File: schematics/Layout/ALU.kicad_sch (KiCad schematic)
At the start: 11 parts

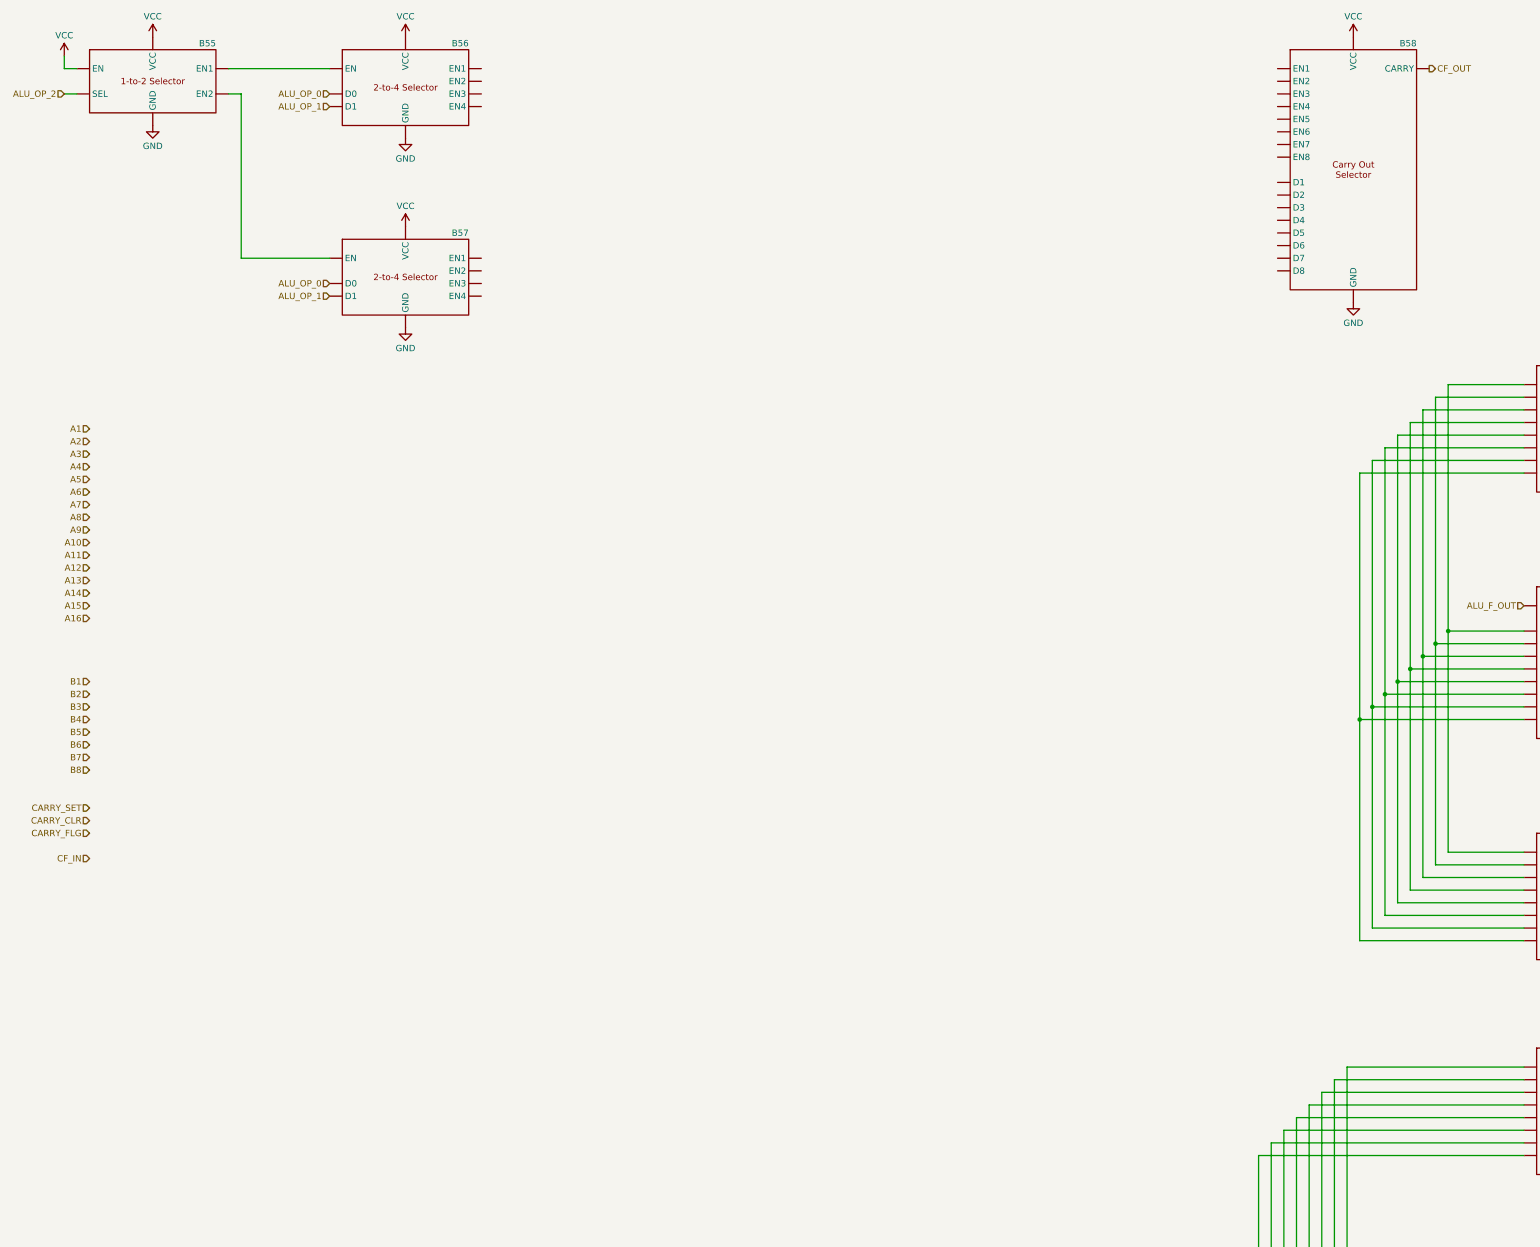
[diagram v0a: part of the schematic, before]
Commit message: Update layout to KiCad 9.0.1, add adder portion of ALU, add 2 bit adder component.
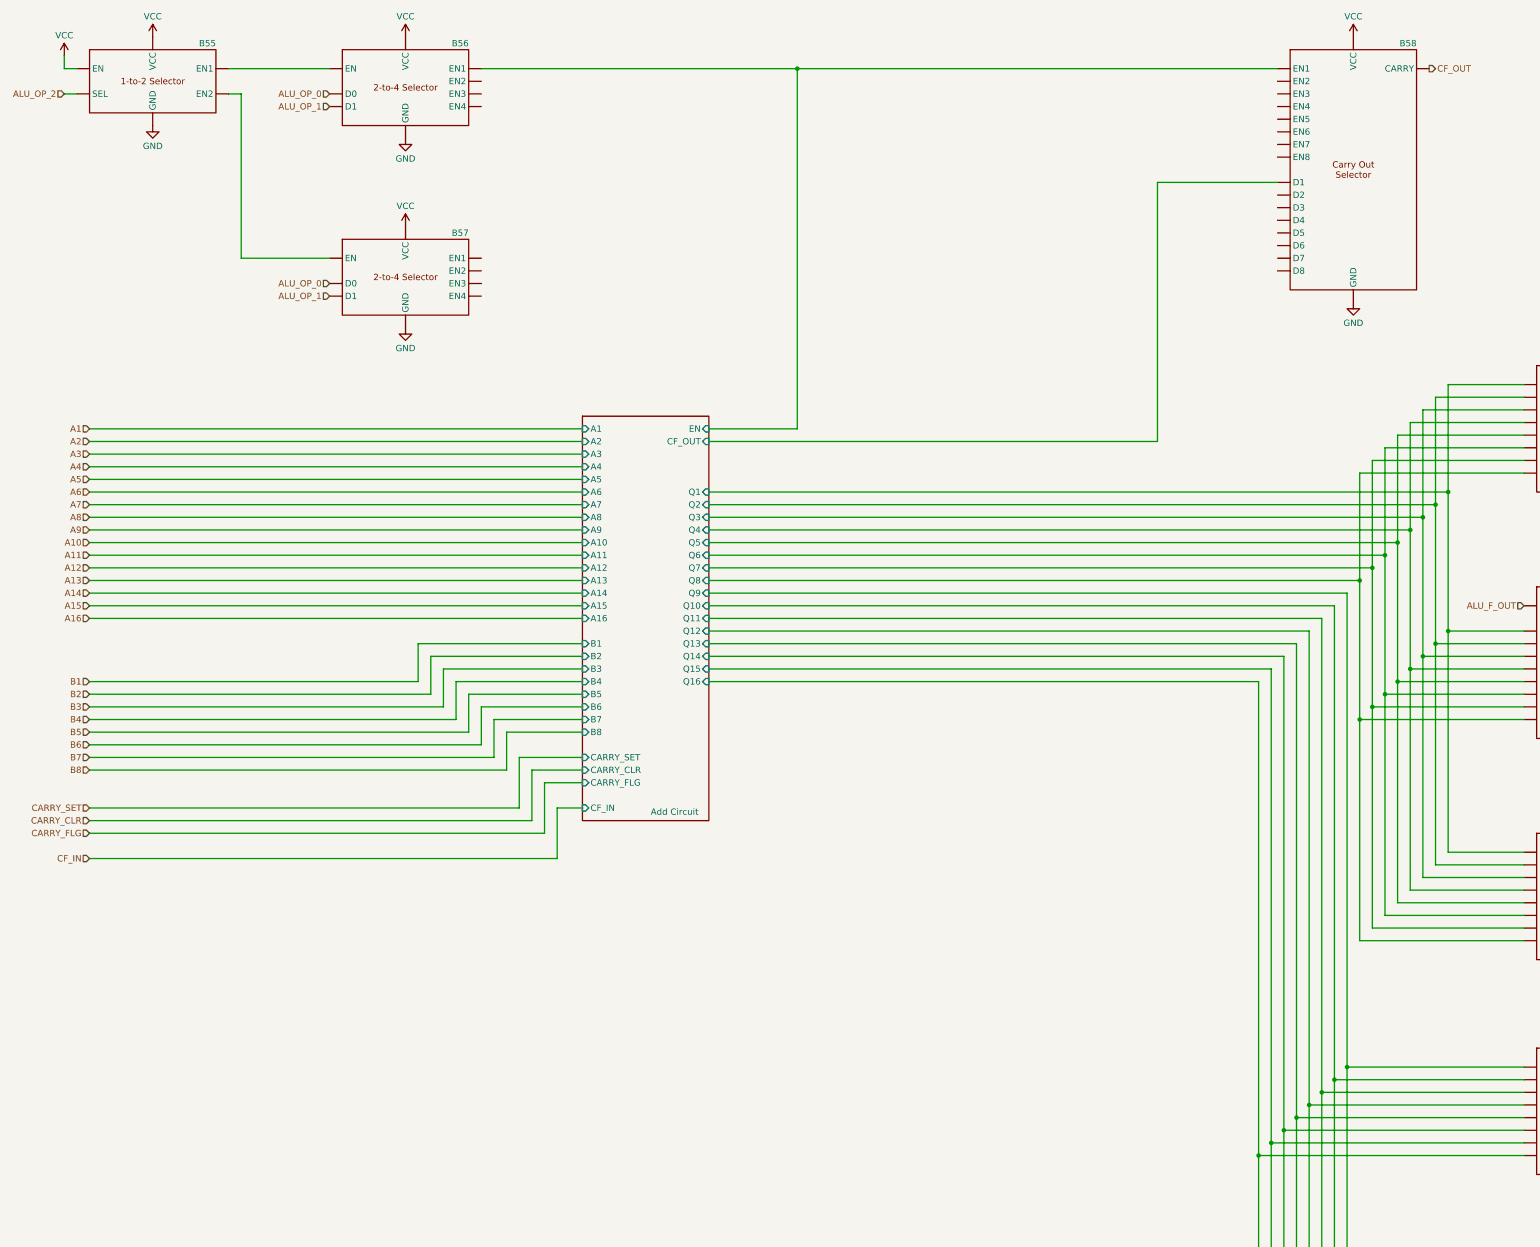
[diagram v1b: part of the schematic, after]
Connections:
- new net: B55. (EN2), B57. (EN4)
- new net: B55. (EN2), B56. (EN4)
- new net: B59. (NONZERO), B60. (OUT)
- new net Add Circuit/CF_OUT: B58. (CARRY)
- new net Add Circuit/EN: B56. (EN4), B58. (CARRY)
- new net Add Circuit/Q1: B59. (NONZERO), B61. (GND), B63. (OUT8)
- new net Add Circuit/Q10: B62. (GND), B64. (OUT8), B65. (OUT8)
- new net Add Circuit/Q11: B62. (GND), B64. (OUT8), B65. (OUT8)
- new net Add Circuit/Q12: B62. (GND), B64. (OUT8), B65. (OUT8)
- new net Add Circuit/Q13: B62. (GND), B64. (OUT8), B65. (OUT8)
- new net Add Circuit/Q14: B62. (GND), B64. (OUT8), B65. (OUT8)
- new net Add Circuit/Q15: B62. (GND), B64. (OUT8), B65. (OUT8)
- new net Add Circuit/Q16: B62. (GND), B64. (OUT8), B65. (OUT8)
- new net Add Circuit/Q2: B59. (NONZERO), B61. (GND), B63. (OUT8)
- new net Add Circuit/Q3: B59. (NONZERO), B61. (GND), B63. (OUT8)
- new net Add Circuit/Q4: B59. (NONZERO), B61. (GND), B63. (OUT8)
- new net Add Circuit/Q5: B59. (NONZERO), B61. (GND), B63. (OUT8)
- new net Add Circuit/Q6: B59. (NONZERO), B61. (GND), B63. (OUT8)
- new net Add Circuit/Q7: B59. (NONZERO), B61. (GND), B63. (OUT8)
- new net Add Circuit/Q8: B59. (NONZERO), B61. (GND), B63. (OUT8)
- new net Add Circuit/Q9: B62. (GND), B64. (OUT8), B65. (OUT8)
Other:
- added sheet Add Circuit (ALU Add Circuit.kicad_sch)

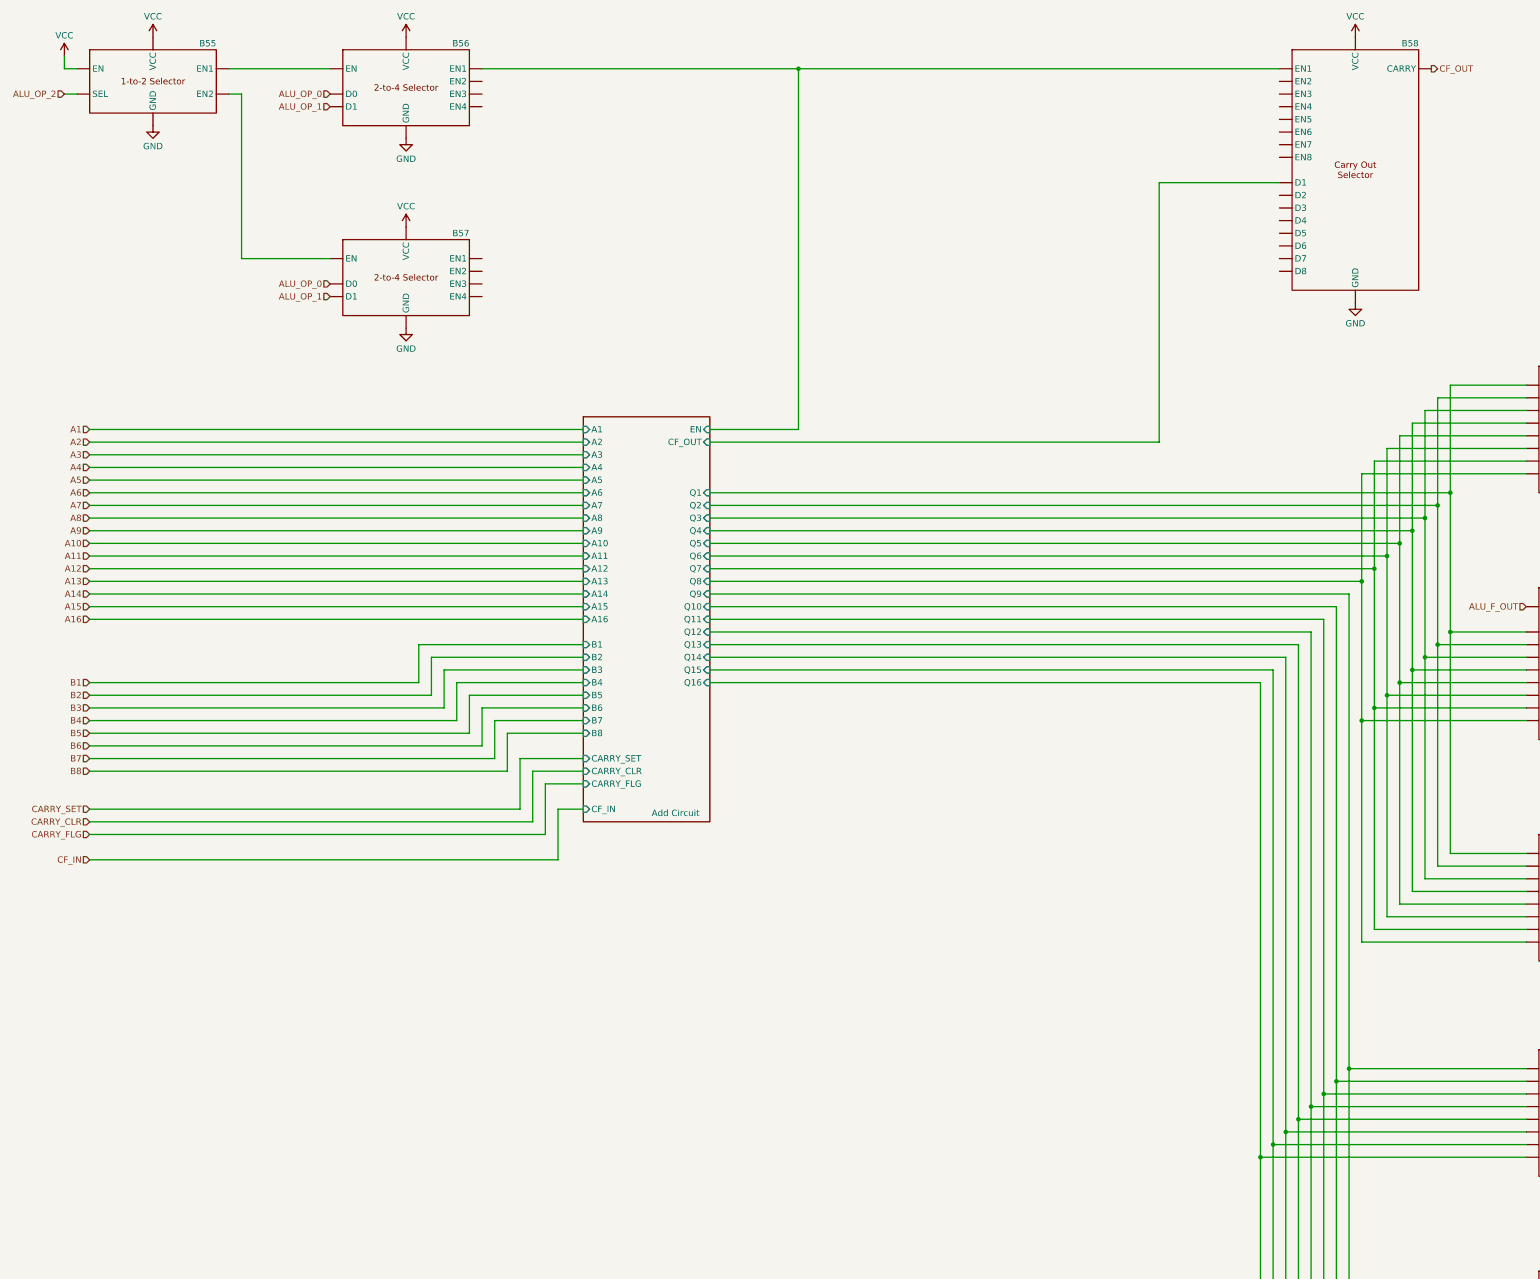
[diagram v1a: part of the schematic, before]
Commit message: Diagram boolean logic board under ALU, new instruction decoder board. Fix backwards ALU opcode decode leftover from swapping to positive instead of inverted signals.
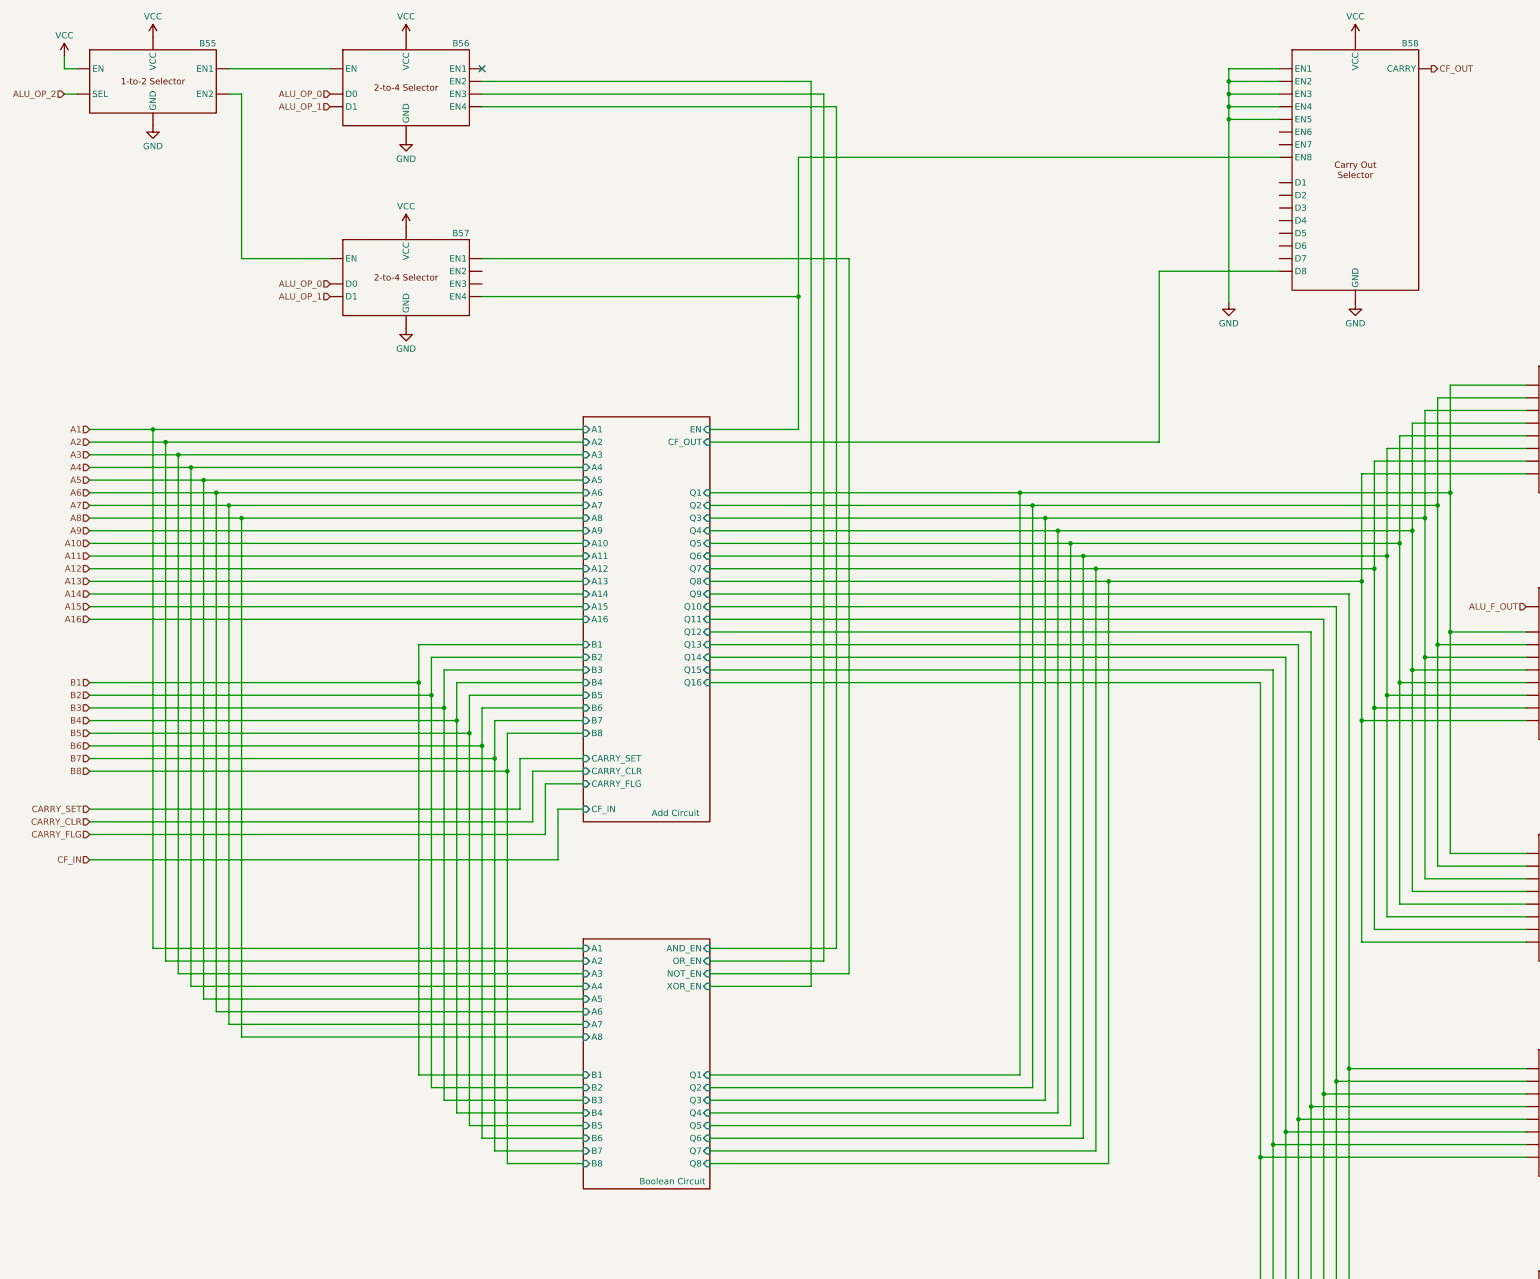
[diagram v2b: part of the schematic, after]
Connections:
- net Add Circuit/EN: now also B57. (EN4); no longer B56. (EN4)
- new net: B55. (EN2), B57. (EN4)
- new net: B55. (EN2), B56. (EN4)
- new net: B59. (NONZERO), B60. (OUT)
- new net Boolean Circuit/AND_EN: B56. (EN4)
- new net Boolean Circuit/NOT_EN: B57. (EN4)
- new net Boolean Circuit/OR_EN: B56. (EN4)
- new net Boolean Circuit/XOR_EN: B56. (EN4)
- no-connect marks 1 -> 2
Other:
- added sheet Boolean Circuit (ALU Boolean Circuit.kicad_sch)
